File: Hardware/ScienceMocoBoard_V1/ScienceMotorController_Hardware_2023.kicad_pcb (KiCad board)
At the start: 2 copper layers, 187 parts, among them J1 RJ45_LED_Shielded, J2 Conn_02x03_Counter_Clockwise, Q1 SI4156DY, Q10 SI4156DY, Q11 SI4156DY, Q12 SI4156DY, Q13 SI4156DY, Q14 SI4156DY, Q15 SI4156DY, Q16 SI4156DY, Q2 SI4156DY, Q3 SI4156DY, Q4 SI4156DY, Q5 SI4156DY, Q6 SI4156DY, Q7 SI4156DY, Q8 SI4156DY, Q9 SI4156DY, SW1 SW_Push, SW10 SW_Push, SW11 SW_DPDT_x2, SW2 SW_Push, SW3 SW_Push, SW4 SW_Push, SW5 SW_Push, SW6 SW_Push, SW7 SW_Push, SW8 SW_Push, SW9 SW_Push, U1 74LVC2G04, U10 IRS2005S, U11 Teensy4.1_DEV-16771, U12 74LVC2G04, U13 IRS2005S, U14 IRS2005S, U15 IRS2005S, U2 IRS2005S, U3 3V3 OKI, U4 TSR_1-2450, U5 74LVC2G04, U6 IRS2005S, U7 IRS2005S, U8 IRS2005S, U9 74LVC2G04

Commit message: Finished buttons, servos, and encoders
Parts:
- moved D3 303.9 mm to (41.4, 113.0), turned to 90 degrees
- moved R3 300.3 mm to (43.3, 113.0), turned to -90 degrees
- moved R10 296.8 mm to (41.4, 104.0)
- moved D9 296.8 mm to (43.3, 104.0), turned to 90 degrees
- moved R11 294.3 mm to (41.7, 95.2), turned to -90 degrees
- moved D8 290.5 mm to (43.6, 95.2), turned to 90 degrees
- moved V2 238.0 mm to (187.9, 158.1)
- moved V1 169.0 mm to (187.9, 50.9)
- moved SW7 151.5 mm to (86.7, 112.5)
- moved R42 150.4 mm to (44.1, 82.2), turned to 0 degrees
- moved DY12 148.5 mm to (40.3, 82.2), turned to 0 degrees
- moved R25 148.2 mm to (89.6, 107.0), turned to -90 degrees
- moved SW11 146.0 mm to (43.2, 73.5), turned to -90 degrees
- moved DY7 144.8 mm to (87.6, 107.0), turned to 90 degrees
- moved SW8 143.1 mm to (77.2, 112.5), turned to 180 degrees
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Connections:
- net Net-(J1-Pad1) renamed /TX+
- net Net-(J1-Pad3) renamed /TX-
- net Net-(J1-Pad4) renamed /RX+
- net Net-(J1-Pad6) renamed /RX-
- U11 pad 3.3V_1: +3.3V -> +3V3
- U11 pad 3.3V_2: +3.3V -> +3V3
- U11 pad 3.3V_3: +3.3V -> +3V3
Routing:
- net +5V: track 0.00 -> 215.7 mm, vias 0 -> 1
- net +3V3: track 332.7 -> 514.9 mm
- net Motor_4_SW: track 0.00 -> 101.3 mm, vias 0 -> 1
- net Motor_3_SW: track 0.00 -> 94.4 mm, vias 0 -> 1
- net Motor_2_SW: track 0.00 -> 87.4 mm, vias 0 -> 1
- net Manual_Control_Right: track 34.0 -> 117.3 mm
- net Servo_4: track 0.00 -> 80.5 mm, vias 0 -> 1
- net Motor_1_SW: track 0.00 -> 80.4 mm, vias 0 -> 1
- net Servo_6: track 0.00 -> 77.7 mm, vias 0 -> 1
- net Manual_Control_Left: track 36.7 -> 111.3 mm
- net Servo_5: track 0.00 -> 71.1 mm, vias 0 -> 1
- net Servo_1: track 0.00 -> 70.5 mm
- net Servo_2: track 0.00 -> 62.4 mm
- net Servo_3: track 0.00 -> 54.2 mm
- net Net-(J1-Pad10): track 0.00 -> 28.8 mm
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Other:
- board text added: "LEFT"
- board text added: "RIGHT"

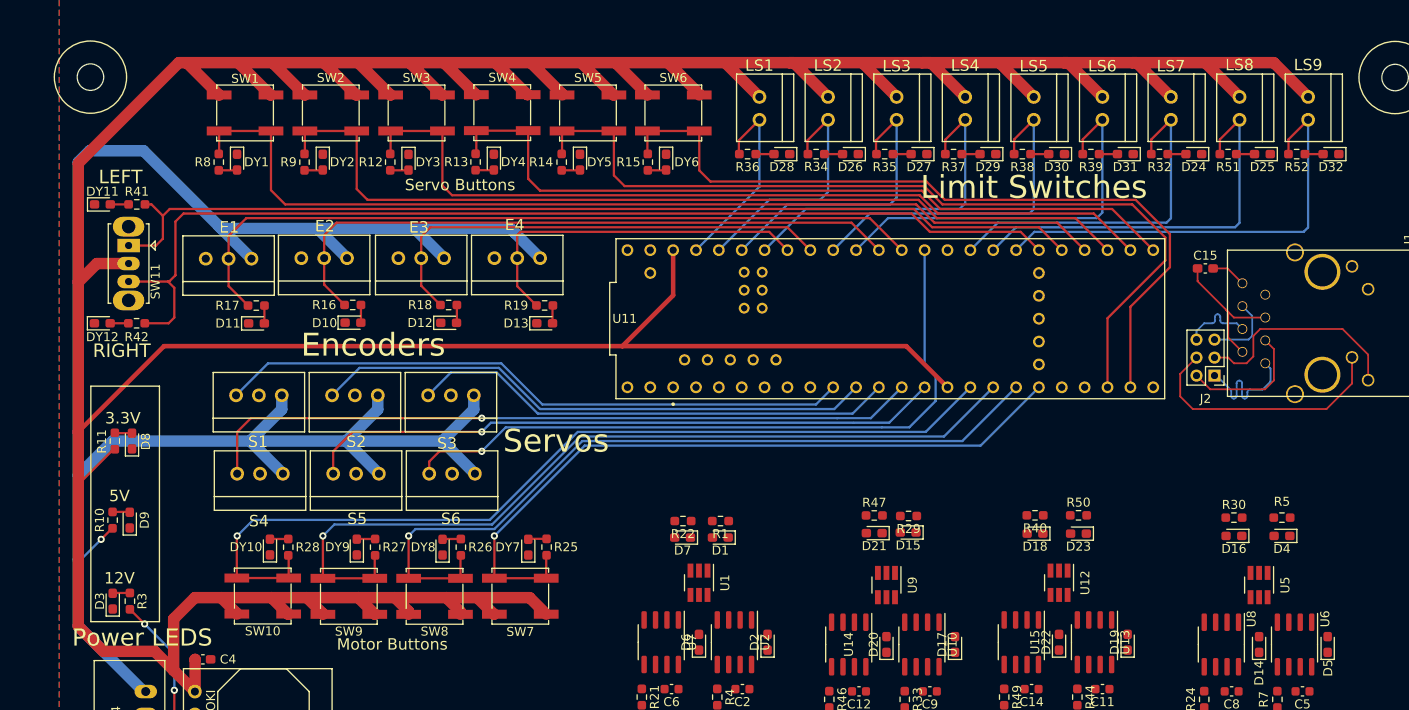
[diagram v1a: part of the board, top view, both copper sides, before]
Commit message: Cleaned up silkscreens
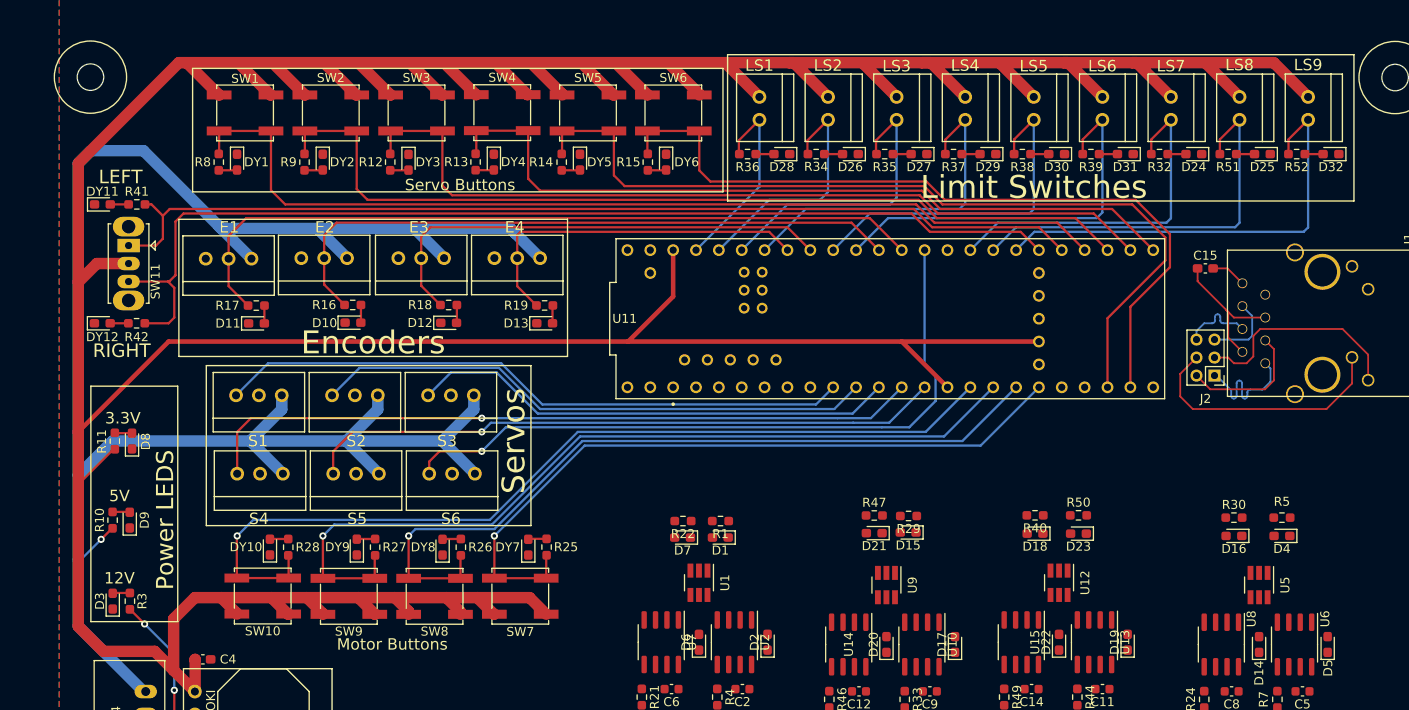
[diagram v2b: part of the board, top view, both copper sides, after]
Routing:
- net +3V3: track 514.9 -> 529.8 mm

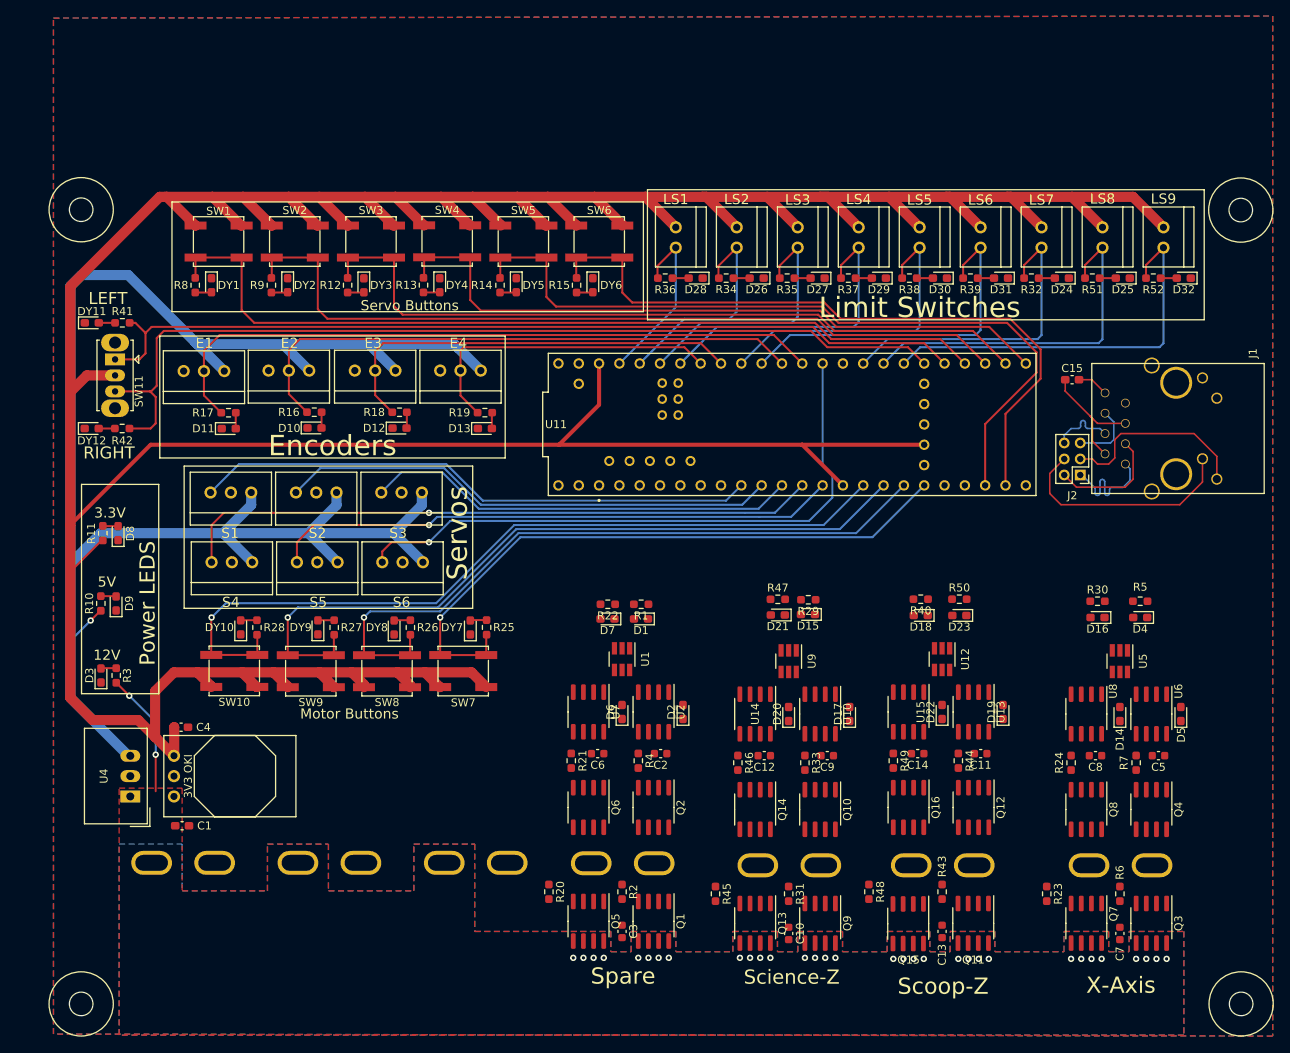
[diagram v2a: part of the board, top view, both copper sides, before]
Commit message: Edge cuts + started H Bridges
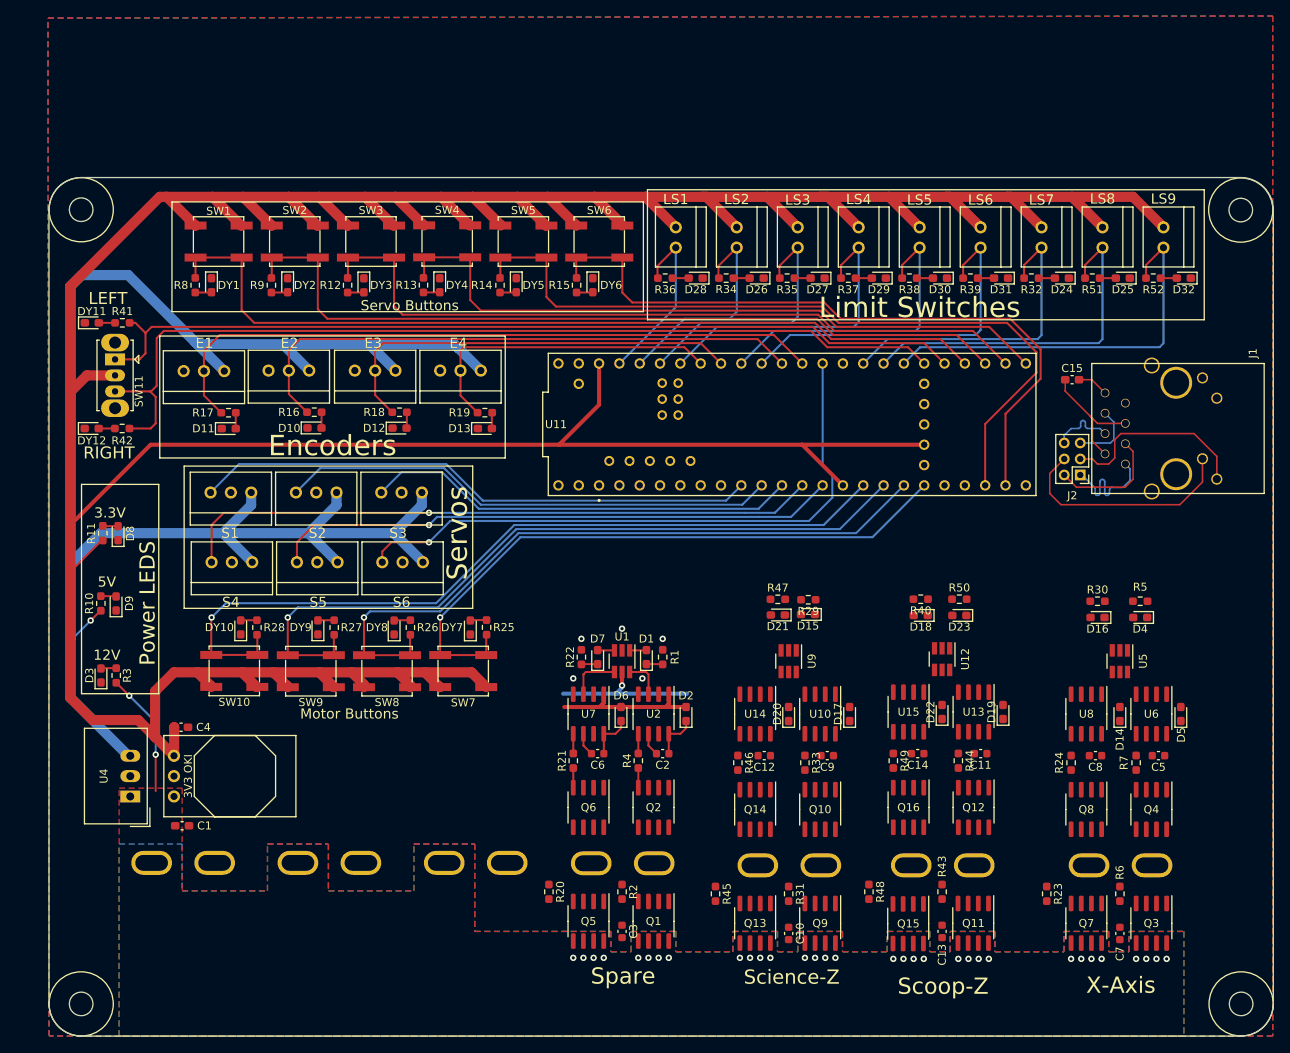
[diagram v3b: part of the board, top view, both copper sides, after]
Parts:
- moved R22 7.38 mm to (101.5, 110.7), turned to -90 degrees
- moved R1 7.13 mm to (111.6, 110.7), turned to 90 degrees
- moved D7 4.93 mm to (103.5, 110.7), turned to 90 degrees
- moved D1 4.82 mm to (109.6, 110.7), turned to 90 degrees
- moved D2 0.46 mm to (114.6, 117.9)
- moved D6 0.28 mm to (106.4, 117.9)
- moved C2 0.25 mm to (111.6, 122.8)
- moved R21 0.25 mm to (100.5, 123.7)
- moved U1 0.25 mm to (106.6, 111.3)
- moved U2 0.25 mm to (110.5, 117.9)
- moved U7 0.25 mm to (102.4, 117.9)
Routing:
- net +12V: track 15.6 -> 34.4 mm
- net +3V3: track 529.8 -> 548.4 mm, vias 0 -> 1
- net Net-(U1-Pad4): track 0.00 -> 6.48 mm
- net Net-(C6-Pad1): track 0.00 -> 5.83 mm
- net Net-(C2-Pad1): track 0.00 -> 5.83 mm
- net Net-(U1-Pad6): track 0.00 -> 4.95 mm
- net /1M-: track 0.00 -> 2.89 mm
- net /1M+: track 0.00 -> 2.89 mm
- net Net-(R4-Pad1): track 0.00 -> 2.45 mm
- net Net-(R21-Pad1): track 0.00 -> 2.45 mm
- net Net-(Q6-Pad4): track 0.00 -> 2.45 mm
- net Net-(Q2-Pad4): track 0.00 -> 2.45 mm
- net RVS_PWM_4: track 0.00 -> 2.11 mm
- net FWD_PWM_4: track 0.00 -> 2.11 mm
- net Net-(D7-Pad1): track 0.00 -> 2.05 mm
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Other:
- board outline added: 153 x 107.3 mm

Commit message: Finished H Bridges
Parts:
- moved R25 82.4 mm to (171.1, 94.8)
- moved DY10 82.4 mm to (140.4, 94.8)
- moved DY7 82.4 mm to (169.1, 94.8)
- moved DY8 82.4 mm to (159.5, 94.8)
- moved R26 82.4 mm to (161.6, 94.8)
- moved R27 82.4 mm to (152.0, 94.8)
- moved SW10 82.4 mm to (139.6, 100.2)
- moved SW9 82.4 mm to (149.1, 100.2)
- moved DY9 82.4 mm to (150.0, 94.8)
- moved R28 82.4 mm to (142.4, 94.8)
- moved SW7 82.4 mm to (168.2, 100.2)
- moved SW8 82.4 mm to (158.6, 100.2)
- moved R11 23.7 mm to (59.3, 111.0), turned to 0 degrees
- moved D8 21.0 mm to (59.3, 109.1), turned to 180 degrees
- moved C7 11.8 mm to (168.7, 133.5), turned to 90 degrees
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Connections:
- C10 pad 1: /1M+ -> /M3+
- C10 pad 2: /1M- -> /M3-
- C11 pad 2: /1M+ -> /M2+
- C12 pad 2: /1M- -> /M3-
- C13 pad 1: /1M+ -> /M2+
- C13 pad 2: /1M- -> /M2-
- C14 pad 2: /1M- -> /M2-
- C2 pad 2: /1M+ -> /M4+
- C3 pad 1: /1M+ -> /M4+
- C3 pad 2: /1M- -> /M4-
- C5 pad 2: /1M+ -> /M1+
- C6 pad 2: /1M- -> /M4-
- C7 pad 1: /1M+ -> /M1+
- C7 pad 2: /1M- -> /M1-
- C8 pad 2: /1M- -> /M1-
- C9 pad 2: /1M+ -> /M3+
- Conn4 pad 1: /1M+ -> /M4+
- Conn4 pad 2: /1M- -> /M4-
- Conn5 pad 1: /1M+ -> /M1+
- Conn5 pad 2: /1M- -> /M1-
- Conn6 pad 1: /1M+ -> /M3+
- Conn6 pad 2: /1M- -> /M3-
- Conn7 pad 1: /1M+ -> /M2+
- Conn7 pad 2: /1M- -> /M2-
- Q1 pad 1: /1M+ -> /M4+
- Q1 pad 2: /1M+ -> /M4+
- Q1 pad 3: /1M+ -> /M4+
- Q10 pad 5: /1M+ -> /M3+
- Q10 pad 6: /1M+ -> /M3+
- Q10 pad 7: /1M+ -> /M3+
- Q10 pad 8: /1M+ -> /M3+
- Q11 pad 1: /1M+ -> /M2+
- Q11 pad 2: /1M+ -> /M2+
- Q11 pad 3: /1M+ -> /M2+
- Q12 pad 5: /1M+ -> /M2+
- Q12 pad 6: /1M+ -> /M2+
- Q12 pad 7: /1M+ -> /M2+
- Q12 pad 8: /1M+ -> /M2+
- Q13 pad 1: /1M- -> /M3-
- Q13 pad 2: /1M- -> /M3-
- Q13 pad 3: /1M- -> /M3-
- Q14 pad 5: /1M- -> /M3-
- Q14 pad 6: /1M- -> /M3-
- Q14 pad 7: /1M- -> /M3-
- Q14 pad 8: /1M- -> /M3-
- Q15 pad 1: /1M- -> /M2-
- Q15 pad 2: /1M- -> /M2-
- Q15 pad 3: /1M- -> /M2-
- Q16 pad 5: /1M- -> /M2-
- Q16 pad 6: /1M- -> /M2-
- Q16 pad 7: /1M- -> /M2-
- Q16 pad 8: /1M- -> /M2-
- Q2 pad 5: /1M+ -> /M4+
- Q2 pad 6: /1M+ -> /M4+
- Q2 pad 7: /1M+ -> /M4+
- Q2 pad 8: /1M+ -> /M4+
- Q3 pad 1: /1M+ -> /M1+
- Q3 pad 2: /1M+ -> /M1+
- Q3 pad 3: /1M+ -> /M1+
- Q4 pad 5: /1M+ -> /M1+
- Q4 pad 6: /1M+ -> /M1+
- Q4 pad 7: /1M+ -> /M1+
- Q4 pad 8: /1M+ -> /M1+
- Q5 pad 1: /1M- -> /M4-
- Q5 pad 2: /1M- -> /M4-
- Q5 pad 3: /1M- -> /M4-
- Q6 pad 5: /1M- -> /M4-
- Q6 pad 6: /1M- -> /M4-
- Q6 pad 7: /1M- -> /M4-
- Q6 pad 8: /1M- -> /M4-
- Q7 pad 1: /1M- -> /M1-
- Q7 pad 2: /1M- -> /M1-
- Q7 pad 3: /1M- -> /M1-
- Q8 pad 5: /1M- -> /M1-
- Q8 pad 6: /1M- -> /M1-
- Q8 pad 7: /1M- -> /M1-
- Q8 pad 8: /1M- -> /M1-
- Q9 pad 1: /1M+ -> /M3+
- Q9 pad 2: /1M+ -> /M3+
- Q9 pad 3: /1M+ -> /M3+
- U10 pad 6: /1M+ -> /M3+
- U11 pad 0: FWD_PWM_1 -> RVS_PWM_4
- U11 pad 1: RVS_PWM_1 -> FWD_PWM_4
- U11 pad 2: FWD_PWM_2 -> RVS_PWM_3
- U11 pad 3: RVS_PWM_2 -> FWD_PWM_3
- U11 pad 4: FWD_PWM_3 -> RVS_PWM_2
- U11 pad 5: RVS_PWM_3 -> FWD_PWM_2
- U11 pad 6: FWD_PWM_4 -> RVS_PWM_1
- U11 pad 7: RVS_PWM_4 -> FWD_PWM_1
- U13 pad 6: /1M+ -> /M2+
- U14 pad 6: /1M- -> /M3-
- U15 pad 6: /1M- -> /M2-
- U2 pad 6: /1M+ -> /M4+
- U6 pad 6: /1M+ -> /M1+
- U7 pad 6: /1M- -> /M4-
- U8 pad 6: /1M- -> /M1-
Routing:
- net +3V3: track 548.4 -> 712.2 mm, vias 1 -> 7
- net +12V: track 34.4 -> 142.6 mm
- net Motor_4_SW: track 101.3 -> 16.4 mm, vias 1 -> 0
- net FWD_PWM_1: track 0.00 -> 84.3 mm, vias 0 -> 3
- net RVS_PWM_1: track 0.00 -> 80.3 mm, vias 0 -> 3
- net Motor_3_SW: track 94.4 -> 21.4 mm
- net FWD_PWM_2: track 0.00 -> 67.4 mm, vias 0 -> 3
- net RVS_PWM_2: track 0.00 -> 63.3 mm, vias 0 -> 3
- net Motor_2_SW: track 87.4 -> 28.4 mm
- net FWD_PWM_3: track 0.00 -> 52.9 mm, vias 0 -> 3
- net RVS_PWM_3: track 0.00 -> 49.0 mm, vias 0 -> 3
- net Motor_1_SW: track 80.4 -> 35.4 mm
- net FWD_PWM_4: track 2.11 -> 37.3 mm, vias 0 -> 3
- net RVS_PWM_4: track 2.11 -> 33.0 mm, vias 0 -> 3
- net Net-(R45-Pad1): track 0.00 -> 26.2 mm
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- added copper zone on F.Cu, net /M1+
- added copper zone on F.Cu, net /M1-
- added copper zone on F.Cu, net /M2+
- added copper zone on F.Cu, net /M2-
- added copper zone on F.Cu, net /M3+
- added copper zone on F.Cu, net /M3-
- added copper zone on F.Cu, net /M4+
- added copper zone on F.Cu, net /M4-
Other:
- board size 153 x 107.3 mm -> 153 x 106.4 mm

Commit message: Stitched planes together
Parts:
- added G***: LOGO, MRDT_Silkscreens:0_MRDT_Logo_30mm, F.Cu at (85.1, 115.6)
- added G***: LOGO, MRDT_Silkscreens:z_sig_Grant_Brinker_30mmx7.3, B.Cu at (160.7, 97.2)
- G***: moved to B.Cu
- moved G*** 240.3 mm to (143.5, 129.5), turned to 180 degrees
- moved C7 7.38 mm to (161.3, 133.5)
- moved C8 7.38 mm to (158.4, 123.1)
- moved D16 7.38 mm to (158.4, 111.0)
- moved Q7 7.38 mm to (157.2, 144.0)
- moved Q8 7.38 mm to (157.2, 129.8)
- moved R24 7.38 mm to (155.3, 124.0)
- moved U8 7.38 mm to (157.2, 118.1)
- moved C5 7.38 mm to (166.5, 123.1)
- moved Conn5 7.38 mm to (166.0, 136.4)
- moved D14 7.38 mm to (161.2, 118.1)
- moved D4 7.38 mm to (164.5, 111.0)
- moved D5 7.38 mm to (169.0, 118.1)
- moved Q3 7.38 mm to (165.3, 144.0)
- moved Q4 7.38 mm to (165.3, 129.8)
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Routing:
- net +3V3: track 712.2 -> 704.4 mm
- net RVS_PWM_1: track 80.3 -> 72.8 mm
- net FWD_PWM_1: track 84.3 -> 76.9 mm
- net +12V: track 142.6 -> 137.6 mm, vias 34 -> 69
- net RVS_PWM_2: track 63.3 -> 59.7 mm
- net FWD_PWM_2: track 67.4 -> 63.8 mm
- net FWD_PWM_3: track 52.9 -> 50.3 mm
- net RVS_PWM_3: track 49.0 -> 46.4 mm
- net GND: vias 81 -> 155
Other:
- board text added: "Science Moco Board, Rev 1 Mars Rover Design Team Missouri S&T, 2023 Ethan Medrow, Grant Brinker"
- board text removed: "Science Moco Board, Rev 1 Mars Rover Design Team Missouri S&T, 2022 Ethan Medrow, Josue Cavasos"
